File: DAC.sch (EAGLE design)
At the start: 73 parts, among them IC1 LM2662, IC2 PCM1793, IC3 OPA2134PA, J1 USBSMD, J2 RCJ-21XXMILL, U1 LDO-TPS78233, U2 PCM2707, Y1 12MHz/20pF

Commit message: Protection res
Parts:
- added LOGO1: LOGO-MANTIS, my:LOGO-MANTIS
- added R20, R21: 22, SparkFun-Resistors:RESISTORPTH-1/4W
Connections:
- new net N$100: C35.2, IC3A.OUT, R17.2, R21.1
- new net N$101: C34.2, IC3B.OUT, R14.2, R20.1
- net OUT_L: now also R21.2; no longer C35.2, IC3A.OUT, R17.2
- net OUT_R: now also R20.2; no longer C34.2, IC3B.OUT, R14.2
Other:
- moved on the sheet: J2A, J2B
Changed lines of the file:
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@@
 <part name="C41" library="SparkFun-Capacitors" deviceset="1.0UF-16V-10%(0603)" device="" value="1.0uF"/>
 <part name="C42" library="SparkFun-Capacitors" deviceset="1.0UF-16V-10%(0603)" device="" value="1.0uF"/>
+<part name="R20" library="SparkFun-Resistors" deviceset="RESISTOR" device="PTH-1/4W" value="22"/>
+<part name="R21" library="SparkFun-Resistors" deviceset="RESISTOR" device="PTH-1/4W" value="22"/>
+<part name="LOGO1" library="my" deviceset="LOGO-MANTIS" device=""/>
 </parts>
 <sheets>
@@
 <instance part="R6" gate="G$1" x="187.96" y="53.34" rot="R90"/>
 <instance part="GND16" gate="1" x="106.68" y="66.04" rot="R180"/>
-<instance part="J2" gate="A" x="350.52" y="109.22"/>
-<instance part="J2" gate="B" x="350.52" y="96.52"/>
+<instance part="J2" gate="A" x="350.52" y="88.9"/>
+<instance part="J2" gate="B" x="350.52" y="76.2"/>
 <instance part="C30" gate="G$1" x="241.3" y="127"/>
 <instance part="C35" gate="G$1" x="276.86" y="132.08" rot="R90"/>
@@
 <instance part="C41" gate="G$1" x="314.96" y="137.16"/>
 <instance part="C42" gate="G$1" x="330.2" y="137.16"/>
+<instance part="R20" gate="G$1" x="307.34" y="45.72"/>
+<instance part="R21" gate="G$1" x="307.34" y="111.76"/>
+<instance part="LOGO1" gate="G$1" x="363.22" y="30.48"/>
 </instances>
 <busses>
@@
 <segment>
 <pinref part="J2" gate="A" pin="S"/>
-<wire x1="347.98" y1="106.68" x2="345.44" y2="106.68" width="0.1524" layer="91"/>
-<label x="345.44" y="106.68" size="1.778" layer="95" rot="R180" xref="yes"/>
+<wire x1="347.98" y1="86.36" x2="345.44" y2="86.36" width="0.1524" layer="91"/>
+<label x="345.44" y="86.36" size="1.778" layer="95" rot="R180" xref="yes"/>
 </segment>
 <segment>
 <pinref part="J2" gate="B" pin="S"/>
-<wire x1="347.98" y1="93.98" x2="345.44" y2="93.98" width="0.1524" layer="91"/>
-<label x="345.44" y="93.98" size="1.778" layer="95" rot="R180" xref="yes"/>
+<wire x1="347.98" y1="73.66" x2="345.44" y2="73.66" width="0.1524" layer="91"/>
+<label x="345.44" y="73.66" size="1.778" layer="95" rot="R180" xref="yes"/>
 </segment>
 <segment>
@@
 <net name="OUT_L" class="2">
 <segment>
-<pinref part="IC3" gate="A" pin="OUT"/>
-<wire x1="284.48" y1="111.76" x2="294.64" y2="111.76" width="0.1524" layer="91"/>
-<wire x1="294.64" y1="111.76" x2="294.64" y2="132.08" width="0.1524" layer="91"/>
-<pinref part="C35" gate="G$1" pin="2"/>
-<wire x1="294.64" y1="132.08" x2="281.94" y2="132.08" width="0.1524" layer="91"/>
-<pinref part="R17" gate="G$1" pin="2"/>
-<wire x1="259.08" y1="142.24" x2="294.64" y2="142.24" width="0.1524" layer="91"/>
-<wire x1="294.64" y1="142.24" x2="294.64" y2="132.08" width="0.1524" layer="91"/>
-<junction x="294.64" y="132.08"/>
-<wire x1="294.64" y1="111.76" x2="299.72" y2="111.76" width="0.1524" layer="91"/>
-<junction x="294.64" y="111.76"/>
-<label x="299.72" y="111.76" size="1.778" layer="95" xref="yes"/>
-</segment>
-<segment>
 <pinref part="J2" gate="B" pin="T"/>
-<wire x1="347.98" y1="96.52" x2="332.74" y2="96.52" width="0.1524" layer="91"/>
-<label x="332.74" y="96.52" size="1.778" layer="95" rot="R180" xref="yes"/>
+<wire x1="347.98" y1="76.2" x2="332.74" y2="76.2" width="0.1524" layer="91"/>
+<label x="332.74" y="76.2" size="1.778" layer="95" rot="R180" xref="yes"/>
+</segment>
+<segment>
+<pinref part="R21" gate="G$1" pin="2"/>
+<wire x1="312.42" y1="111.76" x2="317.5" y2="111.76" width="0.1524" layer="91"/>
+<label x="317.5" y="111.76" size="1.778" layer="95" xref="yes"/>
 </segment>
 </net>
 <net name="OUT_R" class="2">
 <segment>
-<wire x1="281.94" y1="45.72" x2="292.1" y2="45.72" width="0.1524" layer="91"/>
-<wire x1="292.1" y1="45.72" x2="292.1" y2="66.04" width="0.1524" layer="91"/>
-<pinref part="C34" gate="G$1" pin="2"/>
-<wire x1="292.1" y1="66.04" x2="279.4" y2="66.04" width="0.1524" layer="91"/>
-<pinref part="R14" gate="G$1" pin="2"/>
-<wire x1="256.54" y1="76.2" x2="292.1" y2="76.2" width="0.1524" layer="91"/>
-<wire x1="292.1" y1="76.2" x2="292.1" y2="66.04" width="0.1524" layer="91"/>
-<junction x="292.1" y="66.04"/>
-<wire x1="292.1" y1="45.72" x2="297.18" y2="45.72" width="0.1524" layer="91"/>
-<junction x="292.1" y="45.72"/>
-<label x="297.18" y="45.72" size="1.778" layer="95" xref="yes"/>
-<pinref part="IC3" gate="B" pin="OUT"/>
-</segment>
-<segment>
 <pinref part="J2" gate="A" pin="T"/>
-<wire x1="347.98" y1="109.22" x2="332.74" y2="109.22" width="0.1524" layer="91"/>
-<label x="332.74" y="109.22" size="1.778" layer="95" rot="R180" xref="yes"/>
+<wire x1="347.98" y1="88.9" x2="332.74" y2="88.9" width="0.1524" layer="91"/>
+<label x="332.74" y="88.9" size="1.778" layer="95" rot="R180" xref="yes"/>
+</segment>
+<segment>
+<pinref part="R20" gate="G$1" pin="2"/>
+<wire x1="312.42" y1="45.72" x2="320.04" y2="45.72" width="0.1524" layer="91"/>
+<label x="320.04" y="45.72" size="1.778" layer="95" xref="yes"/>
 </segment>
 </net>
@@
 </segment>
 </net>
+<net name="N$100" class="2">
+<segment>
+<pinref part="IC3" gate="A" pin="OUT"/>
+<wire x1="284.48" y1="111.76" x2="294.64" y2="111.76" width="0.1524" layer="91"/>
+<wire x1="294.64" y1="111.76" x2="294.64" y2="132.08" width="0.1524" layer="91"/>
+<pinref part="C35" gate="G$1" pin="2"/>
+<wire x1="294.64" y1="132.08" x2="281.94" y2="132.08" width="0.1524" layer="91"/>
+<pinref part="R17" gate="G$1" pin="2"/>
+<wire x1="259.08" y1="142.24" x2="294.64" y2="142.24" width="0.1524" layer="91"/>
+<wire x1="294.64" y1="142.24" x2="294.64" y2="132.08" width="0.1524" layer="91"/>
+<junction x="294.64" y="132.08"/>
+<wire x1="294.64" y1="111.76" x2="302.26" y2="111.76" width="0.1524" layer="91"/>
+<junction x="294.64" y="111.76"/>
+<pinref part="R21" gate="G$1" pin="1"/>
+</segment>
+</net>
+<net name="N$101" class="2">
+<segment>
+<wire x1="281.94" y1="45.72" x2="292.1" y2="45.72" width="0.1524" layer="91"/>
+<wire x1="292.1" y1="45.72" x2="292.1" y2="66.04" width="0.1524" layer="91"/>
+<pinref part="C34" gate="G$1" pin="2"/>
+<wire x1="292.1" y1="66.04" x2="279.4" y2="66.04" width="0.1524" layer="91"/>
+<pinref part="R14" gate="G$1" pin="2"/>
+<wire x1="256.54" y1="76.2" x2="292.1" y2="76.2" width="0.1524" layer="91"/>
+<wire x1="292.1" y1="76.2" x2="292.1" y2="66.04" width="0.1524" layer="91"/>
+<junction x="292.1" y="66.04"/>
+<wire x1="292.1" y1="45.72" x2="302.26" y2="45.72" width="0.1524" layer="91"/>
+<junction x="292.1" y="45.72"/>
+<pinref part="IC3" gate="B" pin="OUT"/>
+<pinref part="R20" gate="G$1" pin="1"/>
+</segment>
+</net>

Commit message: Some packages updated
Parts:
- IC1: device my:MAX1044 -> my:LM2662
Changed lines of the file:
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@@
 <part name="GB1" library="my" deviceset="COPPER-BRIDGE" device="" value=""/>
 <part name="GND19" library="SparkFun-Aesthetics" deviceset="GND" device=""/>
-<part name="IC1" library="my" deviceset="MAX1044" device="" value="LM2662"/>
+<part name="IC1" library="my" deviceset="LM2662" device="" value="LM2662"/>
 <part name="C21" library="SparkFun-Capacitors" deviceset="1.0UF-16V-10%(0603)" device="" value="1.0uF"/>
 <part name="C17" library="SparkFun-Capacitors" deviceset="CAP_POL" device="PTH2" value="10uF"/>

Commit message: Phone out
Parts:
- added C43, C44: 100pF, SparkFun-Capacitors:CAPPTH
- added C45, C46: 1.0uF, SparkFun-Capacitors:1.0UF-16V-10%(0603)
- added IC4: LMH6643, my:LMH6643
- added J3: (no value), SparkFun-Connectors:AUDIO-JACK2.5MM
- added R22: TD90, my:TD90
- added R23, R26: 3.3k, SparkFun-Resistors:RESISTORPTH-1/4W
- added R24, R27: 1.8k, SparkFun-Resistors:RESISTORPTH-1/4W
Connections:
- net N$6 renamed D+*
- net N$7 renamed D-*
- removed net N$100: C35.2, IC3A.OUT, R17.2, R21.1
- removed net N$101: C34.2, IC3B.OUT, R14.2, R20.1
- new net HP_L: C43.1, IC4A.OUT, J3.LEFT, R23.2
- new net HP_R: C44.1, IC4B.OUT, J3.RIGHT, R26.2
- new net N$12: IC4A.+IN, R22A.S
- new net N$14: C43.2, IC4A.-IN, R23.1, R24.2
- new net N$15: IC4B.+IN, R22B.S
- new net N$19: C44.2, IC4B.-IN, R26.1, R27.2
- new net OUT_L*: C35.2, IC3A.OUT, R17.2, R21.1, R22A.E
- new net OUT_R*: C34.2, IC3B.OUT, R14.2, R20.1, R22B.E
- net +5V: now also C46.1, IC4A.V+
- net -5V: now also C45.1, IC4A.V-
- net AGND: now also C45.2, C46.2, J3.SLEEVE, R22A.A, R22B.A, R24.1, R27.1

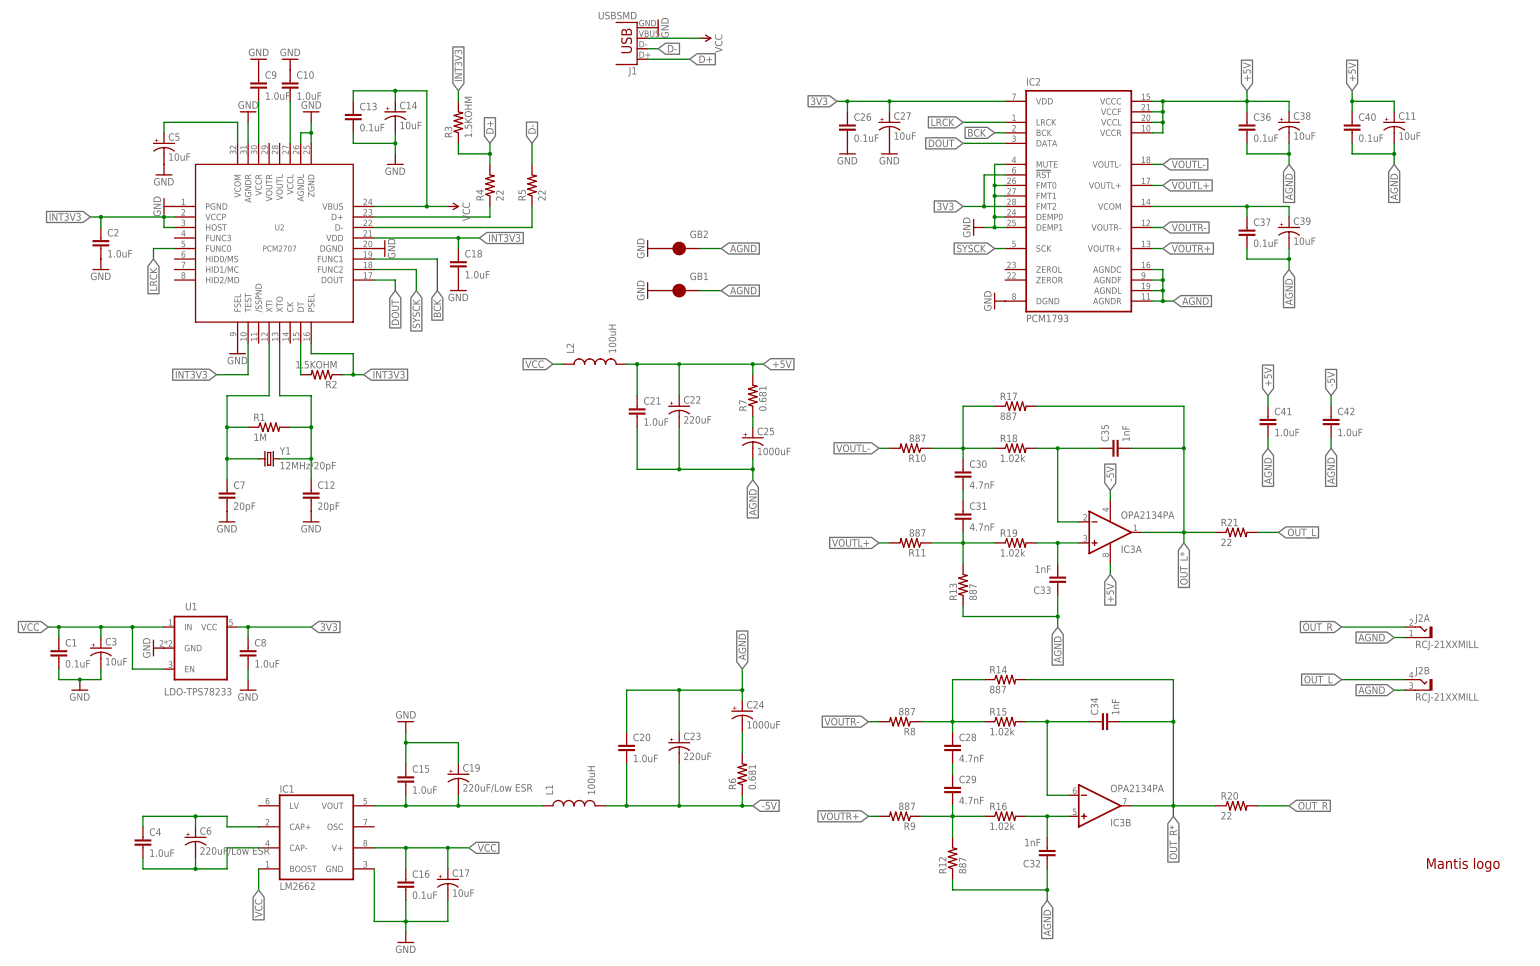
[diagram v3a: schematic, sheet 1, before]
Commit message: Bias correction
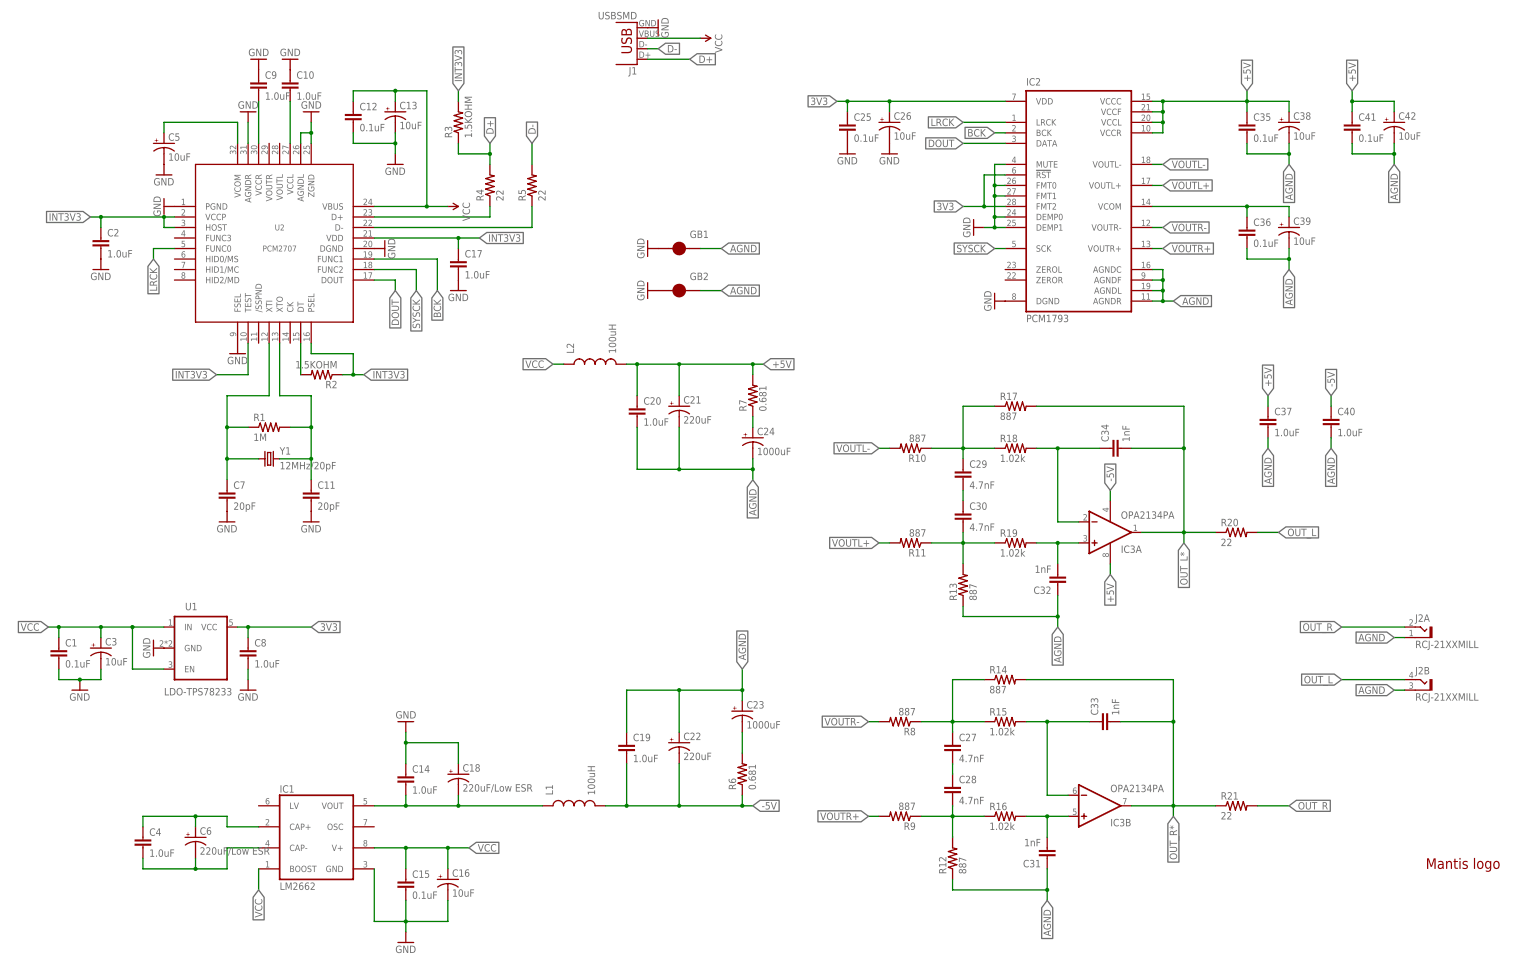
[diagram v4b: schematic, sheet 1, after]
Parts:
- added R25, R28: 3.3k, SparkFun-Resistors:RESISTORPTH-1/4W
- C11: value 10uF -> 20pF; device SparkFun-Capacitors:CAP_POLPTH2 -> SparkFun-Capacitors:18PF-50V-5%(0603)
- C12: value 20pF -> 0.1uF; device SparkFun-Capacitors:18PF-50V-5%(0603) -> SparkFun-Capacitors:0.1UF-25V-5%(0603)
- C13, C16, C26: value 0.1uF -> 10uF; device SparkFun-Capacitors:0.1UF-25V-5%(0603) -> SparkFun-Capacitors:CAP_POLPTH2
- C14, C17: value 10uF -> 1.0uF; device SparkFun-Capacitors:CAP_POLPTH2 -> SparkFun-Capacitors:1.0UF-16V-10%(0603)
- C15, C41: value 1.0uF -> 0.1uF; device SparkFun-Capacitors:1.0UF-16V-10%(0603) -> SparkFun-Capacitors:0.1UF-25V-5%(0603)
- C18: value 1.0uF -> 220uF/Low ESR; device SparkFun-Capacitors:1.0UF-16V-10%(0603) -> rcl:CPOL-USE3.5-8
- C19: value 220uF/Low ESR -> 1.0uF; device rcl:CPOL-USE3.5-8 -> SparkFun-Capacitors:1.0UF-16V-10%(0603)
- C21: value 1.0uF -> 220uF; device SparkFun-Capacitors:1.0UF-16V-10%(0603) -> rcl:CPOL-USE3.5-8; PACKAGE (none) -> 8/3.5
- C23: value 220uF -> 1000uF; device rcl:CPOL-USE3.5-8 -> SparkFun-Capacitors:CAP_POLPTH4; PACKAGE 8/3.5 -> (none)
- C25: value 1000uF -> 0.1uF; device SparkFun-Capacitors:CAP_POLPTH4 -> SparkFun-Capacitors:0.1UF-25V-5%(0603)
- C27: value 10uF -> 4.7nF; device SparkFun-Capacitors:CAP_POLPTH2 -> capacitor-wima:C5/4.5
- C31: value 4.7nF -> 1nF; device capacitor-wima:C5/4.5 -> capacitor-wima:C5/2.5
- C35: value 1nF -> 0.1uF; device capacitor-wima:C5/2.5 -> SparkFun-Capacitors:0.1UF-25V-5%(0603)
- C37, C40: value 0.1uF -> 1.0uF; device SparkFun-Capacitors:0.1UF-25V-5%(0603) -> SparkFun-Capacitors:1.0UF-16V-10%(0603)
- C42: value 1.0uF -> 10uF; device SparkFun-Capacitors:1.0UF-16V-10%(0603) -> SparkFun-Capacitors:CAP_POLPTH2
- C44: value 100pF -> 1.0uF; device SparkFun-Capacitors:CAPPTH -> SparkFun-Capacitors:1.0UF-16V-10%(0603)
- C46: value 1.0uF -> 100pF; device SparkFun-Capacitors:1.0UF-16V-10%(0603) -> SparkFun-Capacitors:CAPPTH
- R23, R26: value 3.3k -> 1.3k
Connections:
- new net N$6: IC4B.-IN, R26.2
- new net N$7: IC4A.-IN, R23.2
- net +5V: now also C20.1, C21.+, C35.1, C37.1, C42.+, C45.1; no longer C11.+, C21.1, C22.+, C36.1, C40.1, C46.1
- net -5V: now also C19.2, C22.-, C40.1, C44.1; no longer C20.2, C23.-, C42.1, C45.1
- net 3V3: now also C25.1, C26.+; no longer C26.1, C27.+
- net AGND: now also C19.1, C20.2, C21.-, C22.+, C24.-, C31.1, C35.2, C42.-, C44.2; no longer C11.-, C20.1, C21.2, C22.-, C24.+, C25.-, C33.1, C42.2, C46.2
- net GND: now also C11.2, C13.-, C14.1, C15.2, C16.-, C17.2, C18.+, C25.2, C26.-; no longer C13.2, C14.-, C15.1, C16.2, C17.-, C18.2, C19.+, C26.2, C27.-
- net HP_L: now also R25.2; no longer R23.2
- net HP_R: now also C46.1, R28.2; no longer C44.1, R26.2
- net INT3V3: now also C17.1; no longer C18.1
- net N$10: now also C23.-; no longer C24.-
- net N$14: now also R25.1; no longer IC4A.-IN
- net N$16: now also C29.2, C30.1; no longer C30.2, C31.1
- net N$17: now also C30.2; no longer C31.2
- net N$18: now also C29.1; no longer C30.1
- net N$19: now also C46.2, R28.1; no longer C44.2, IC4B.-IN
- net N$20: now also C28.2; no longer C29.2
- net N$21: now also C27.1; no longer C28.1
- net N$22: now also C27.2, C28.1; no longer C28.2, C29.1
- net N$5: now also C36.1; no longer C37.1
- net N$8: now also C24.+; no longer C25.+
- net N$9: now also C14.2, C18.-; no longer C15.2, C19.-
- net OPL+: now also C32.2; no longer C33.2
- net OPL-: now also C34.1; no longer C35.1
- net OPR+: now also C31.2; no longer C32.2
- net OPR-: now also C33.1; no longer C34.1
- net OUT_L: now also R20.2; no longer R21.2
- net OUT_L*: now also C34.2, R20.1; no longer C35.2, R21.1
- net OUT_R: now also R21.2; no longer R20.2
- net OUT_R*: now also C33.2, R21.1; no longer C34.2, R20.1
- net VCC: now also C12.1, C13.+, C15.1, C16.+; no longer C13.1, C14.+, C16.1, C17.+
- net XTO: now also C11.1; no longer C12.1
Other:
- moved on the sheet: C12, C15, C20, C22, C23, C24, C28, C29, C30, C31, C32, C33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
